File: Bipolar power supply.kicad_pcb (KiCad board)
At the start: 2 copper layers, 100 x 70 mm, 37 parts, among them J1 Screw #6-32, J2 Screw #6-32, J3 Screw #6-32, J4 Conn_01x03, U1 LM317_TO-220, U2 LM337_TO-220

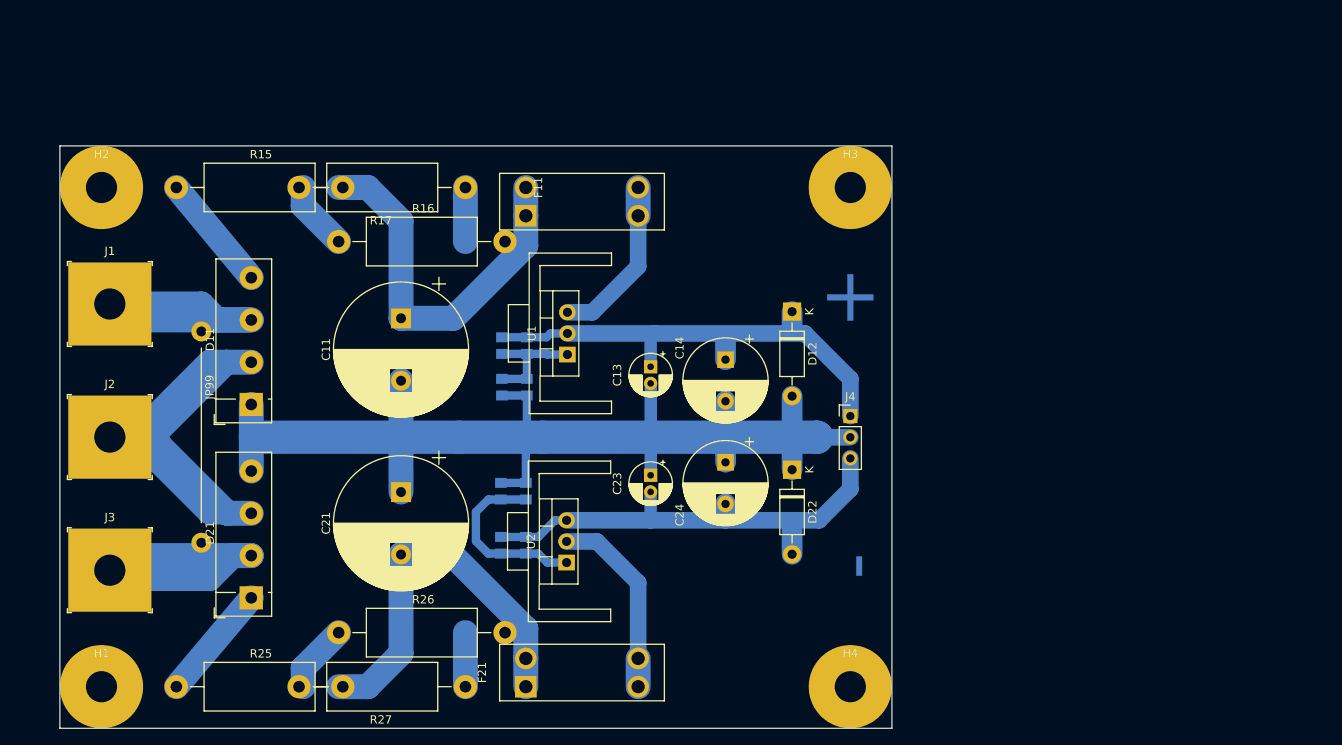
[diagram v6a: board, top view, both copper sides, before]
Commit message: Added LEDs and edge clearance. Rerouted.
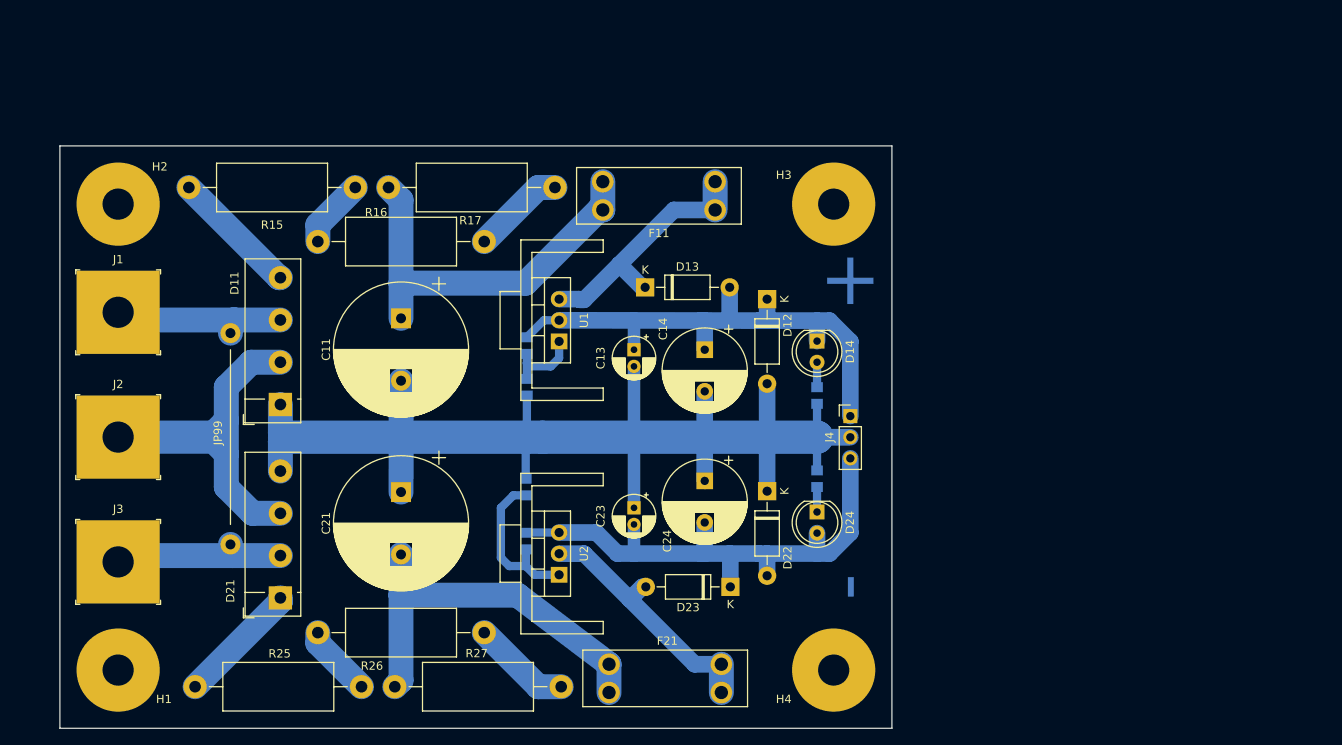
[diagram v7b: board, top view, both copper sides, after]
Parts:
- removed R13, R23: 249, $Local:R_0805_2012Metric_Pad1.20x1.40mm_HandSolder
- added D13: 1N4007T, Diode_THT:D_DO-41_SOD81_P10.16mm_Horizontal, F.Cu at (120.3, 82.0)
- added D14: LED, $Local:LED_D5.0mm, F.Cu at (141.0, 88.5)
- added D23: 1N4007T, Diode_THT:D_DO-41_SOD81_P10.16mm_Horizontal, F.Cu at (130.6, 118.0)
- added D24: LED, $Local:LED_D5.0mm, F.Cu at (141.0, 109.0)
- moved R24 38.0 mm to (141.0, 105.0)
- moved R14 37.9 mm to (141.0, 95.0)
- moved R27 11.5 mm to (110.2, 130.0)
- moved R17 10.8 mm to (109.5, 70.0)
- moved F21 10.0 mm to (122.8, 129.0)
- moved F11 9.28 mm to (122.0, 71.0)
- moved C23 4.39 mm to (119.0, 108.5)
- moved D22 3.96 mm to (135.0, 106.5)
- moved JP99 3.51 mm to (70.5, 87.5)
- moved D11 3.50 mm to (76.5, 96.1)
- moved D21 3.50 mm to (76.5, 119.3)
- moved D12 3.35 mm to (135.0, 83.4)
- moved C24 3.35 mm to (127.5, 105.3)
- moved C13 2.86 mm to (119.0, 89.5)
- moved H1 2.83 mm to (57.0, 128.0)
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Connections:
- R14 pad 1: /ADJ_P -> Net-(R14-Pad1)
- R24 pad 2: /ADJ_N -> Net-(R24-Pad2)
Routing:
- net /CT: track 63.1 -> 44.2 mm
- net /AC_N: track 36.3 -> 21.3 mm
- net /AC_P: track 35.6 -> 21.6 mm
- net /GND: track 141.3 -> 152.5 mm
- net /VNEG: track 55.5 -> 66.4 mm
- net /IN_P: track 20.3 -> 30.9 mm
- net /VPOS: track 56.8 -> 65.8 mm
- net Net-(R25-Pad2): track 0.00 -> 8.67 mm
- net /IN_N: track 23.2 -> 30.9 mm
- net Net-(C21-Pad2): track 55.0 -> 47.4 mm
- net Net-(R26-Pad2): track 6.50 -> 11.9 mm
- net Net-(R16-Pad2): track 6.50 -> 11.2 mm
- net /ADJ_P: track 13.9 -> 9.44 mm
- net Net-(R24-Pad2): track 0.00 -> 3.00 mm
- net Net-(R14-Pad1): track 0.00 -> 3.00 mm
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
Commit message: Switched to non-CT transformer. Redesigned and rerouted.
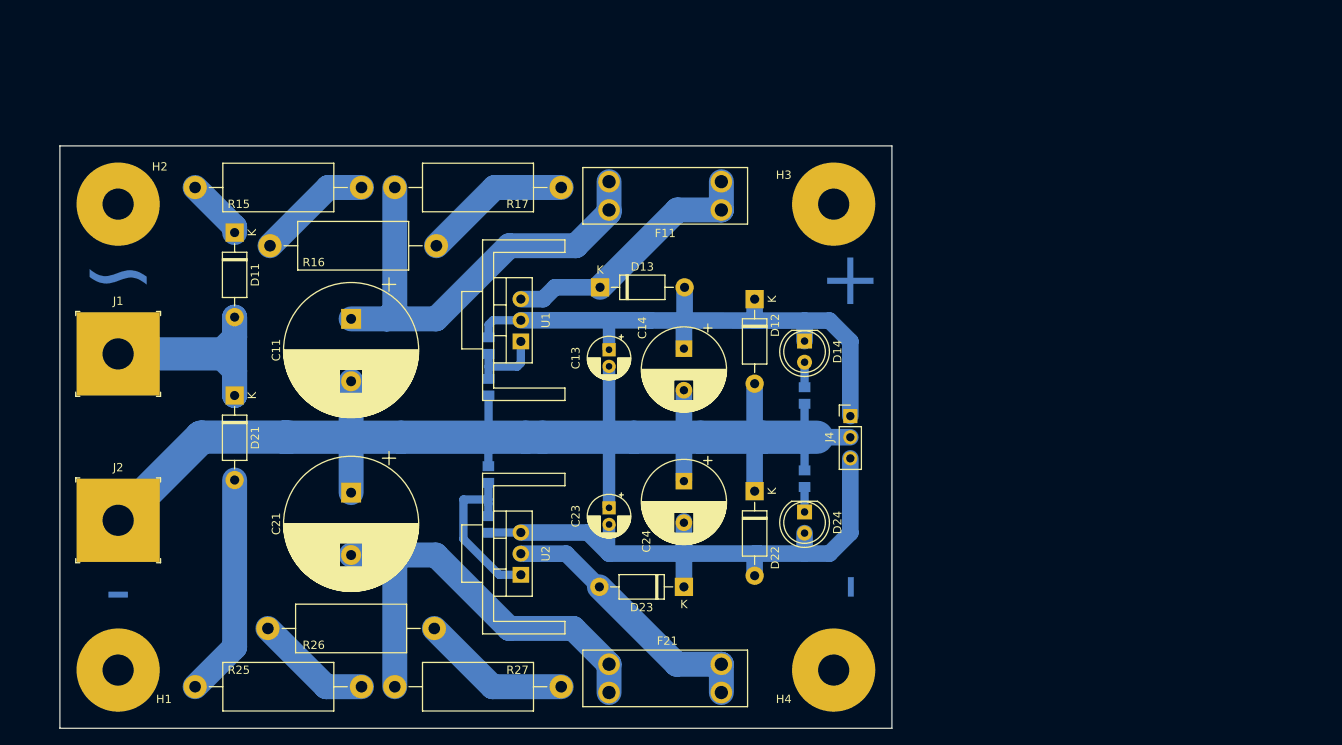
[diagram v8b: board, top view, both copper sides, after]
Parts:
- removed J3: Screw #6-32, $Local:ScrewTerminal_01x01_#6-32_10mm
- removed JP99: Open, $Local:Jumper_P25.40mm
- D11, D21: value KBL06 -> 1N4007T; footprint Diode_THT:Diode_Bridge_Vishay_KBL -> Diode_THT:D_DO-41_SOD81_P10.16mm_Horizontal
- moved D21 24.9 mm to (71.0, 95.0), turned to -90 degrees
- moved D11 21.4 mm to (71.0, 75.4), turned to -90 degrees
- moved J2 10.0 mm to (57.0, 110.0)
- moved R26 6.02 mm to (75.0, 123.0)
- moved C11 6.00 mm to (85.0, 85.8)
- moved C21 6.00 mm to (85.0, 106.7)
- moved R16 5.77 mm to (75.2, 77.0)
- moved D23 5.58 mm to (125.0, 118.0)
- moved D13 5.42 mm to (114.9, 82.0)
- moved J1 5.00 mm to (57.0, 90.0)
- moved R21 4.92 mm to (101.5, 110.5), turned to -90 degrees
- moved R22 4.74 mm to (101.5, 104.5)
- moved R11 4.60 mm to (101.5, 89.0)
- moved R12 4.60 mm to (101.5, 94.0)
- moved U1 4.60 mm to (105.4, 88.5)
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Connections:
- D11 pad 1: /GND -> Net-(R15-Pad1)
- D11 pad 2: /CT -> /AC
- D21 pad 1: Net-(D21-Pad1) -> /AC
- D21 pad 2: /AC_N -> Net-(R25-Pad1)
- J1 pad 1: /AC_P -> /AC
- J2 pad 1: /CT -> /GND
- R15 pad 1: Net-(D11-Pad4) -> Net-(R15-Pad1)
- R25 pad 1: Net-(D21-Pad1) -> Net-(R25-Pad1)
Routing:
- net /CT: track 44.2 -> 0.00 mm
- net /AC: track 0.00 -> 32.5 mm
- net Net-(R25-Pad1): track 0.00 -> 26.8 mm
- net /AC_P: track 21.6 -> 0.00 mm
- net /AC_N: track 21.3 -> 0.00 mm
- net /GND: track 152.5 -> 168.1 mm
- net Net-(D11-Pad4): track 15.5 -> 0.00 mm
- net Net-(D21-Pad1): track 14.9 -> 0.00 mm
- net Net-(C11-Pad1): track 47.6 -> 56.2 mm
- net Net-(C21-Pad2): track 47.4 -> 55.7 mm
- net Net-(R15-Pad1): track 0.00 -> 7.39 mm
- net Net-(R16-Pad2): track 11.2 -> 17.9 mm
- net Net-(R26-Pad2): track 11.9 -> 18.1 mm
- net Net-(R15-Pad2): track 8.36 -> 13.9 mm
- net Net-(R25-Pad2): track 8.67 -> 14.1 mm
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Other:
- board text added: "~"
